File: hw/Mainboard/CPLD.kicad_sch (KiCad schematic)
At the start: 48 parts, among them J21 FPGA-P4, J22 Conn_02x15_Odd_Even, J23 FPGA_P2, J24 FPGA_P3, Q4 MMBT3904, SW5 CONFIG, U21 T8Q144C3, X1 50MHZ

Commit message: hw: wip
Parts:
- removed J22: Conn_02x15_Odd_Even, Connector_PinHeader_2.54mm:PinHeader_2x15_P2.54mm_Vertical, symbol Connector_Generic:Conn_02x15_Odd_Even
- added C82: 100n, Capacitor_SMD:C_0402_1005Metric, symbol Device:C_Small
- added J19: PROG, Connector_IDC:IDC-Header_2x08_P2.54mm_Vertical, symbol Connector_Generic:Conn_02x08_Odd_Even
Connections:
- net +3V3: now also C82.1, J19.1 (Pin_1)
- net CDONE: now also J19.10 (Pin_10)
- net GND: now also C82.2
- net NSTATUS: now also J19.5 (Pin_5)
- net SPI0_RX: now also J19.2 (Pin_2)
- net SPI0_SCK: now also J19.6 (Pin_6)
- net SPI0_TX: now also J19.4 (Pin_4)
- net SPI0_~{CS}: now also J19.8 (Pin_8)
- net TCK: now also RN14.3 (R3.1), J19.13 (Pin_13); no longer RN14.1 (R1.1)
- net TDI: now also RN14.4 (R4.1), J19.15 (Pin_15); no longer RN14.2 (R2.1)
- net TDO: now also RN14.1 (R1.1), J19.9 (Pin_9); no longer RN14.3 (R3.1)
- net TMS: now also RN14.2 (R2.1), J19.11 (Pin_11); no longer RN14.4 (R4.1)
- net ~{CRESET}: now also J19.12 (Pin_12)
- net ~{FPGA_PROG}: now also J19.16 (Pin_16)
- new net HOLD: J19.14 (Pin_14)
- new net PD_GND: J19.7 (Pin_7)
- no-connect marks 28 -> 29
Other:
- note added: "AD6"

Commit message: hw: larger schematic pages, routed w/netties
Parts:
- removed R48, R51, R63, R67: 10k, Resistor_SMD:R_0402_1005Metric, symbol Device:R_Small
- added RN15: 10k, Resistor_SMD:R_Array_Convex_4x0603, symbol Device:R_Pack04
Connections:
- net +3V3: now also J19.3 (Pin_3), RN15.5 (R4.2), RN15.6 (R3.2), RN15.7 (R2.2), RN15.8 (R1.2); no longer J19.1 (Pin_1)
- net CBUS0: now also RN15.1 (R1.1)
- net CBUS1: now also RN15.2 (R2.1)
- net CBUS2: now also RN15.3 (R3.1)
- net CSI: now also RN15.4 (R4.1)
- net SPI1_~{READY}: now also U21.18 (GPIOL_20_CTRL0_CDI4)
- no-connect marks 29 -> 30
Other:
- note added: "CDONE is open drain"
- note removed: "CDONE is an open drain"
- moved on the sheet: C59, C60, C61, C62, C63, C64, C65, C66, C67, C68, C69, C70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

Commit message: hw: wip
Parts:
- added NT39: +3V3, PET:NetTie-2_SMD_Pad_1.6_to_0.4mm, symbol PET:PowerTie_2
- added NT40, NT43, NT44: +3V3, PET:NetTie-2_SMD_Pad_0.4_to_0.28mm, symbol PET:PowerTie_2
- added PT3: PowerTie_2, PET:NetTie-2_SMD_Pad_1.6_to_0.4mm, symbol PET:PowerTie_2
- NT7, NT8: footprint PET:NetTie-2_SMD_Pad_0.4_to_0.2mm -> PET:NetTie-2_SMD_Pad_0.4_to_0.28mm; symbol Device:NetTie_2 -> PET:PowerTie_2
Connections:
- net +3V3: now also NT7.1, NT39.2, NT40.1, PT3.2; no longer NT7.2
- net FPGA_VCC: now also NT43.2, NT44.2
- net FPGA_VCCIO: now also NT7.2, NT40.2; no longer NT7.1
- net GRAPHICS: now also J23.14 (Pin_14), U21.45 (GPIOB_TXP06); no longer J23.13 (Pin_13), U21.43 (GPIOB_TXN04)
- net VIA_CB2: now also J23.13 (Pin_13), U21.43 (GPIOB_TXN04); no longer J23.14 (Pin_14), U21.45 (GPIOB_TXP06)
- net MCU_CEC: now reaches U21.33 (GPIOL_05_CSO)
- net ~{FPGA_PROG} renamed ~{SPI_ENA}
- new net +1V2: NT43.1, NT44.1
- new net PD_3V3: NT39.1, PT3.1
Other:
- note added: "Pull ~{CRESET} low to reset FPGA until MCU is ready Pull CSI high to enable FPGA configuration Pull TEST_N high to deactivate test mode Pull CBUS[2:0] high for 1x SPI width Leave CBSEL[1:0] floating (not using multi-image) MCU config: MCU drives SS_N low to select passive SPI MCU transitions CRESET_N low -> high to begin (320 ns) MCU sends bitsteam via CCK and CDI0 FPGA asserts CDONE on success, 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"
- note removed: "Pull CSI high to enable FPGA configuration Pull TEST_N high to deactivate test mode Pull CBUS[2:1] high as we don't support more than 2x Leave CBSEL[1:0] floating CRESET_N pulled low to reset FPGA until MCU is ready Config sequence: MCU drives CBUS[0] high for 1x or low for 2x MCU drives SS_N low to select passive SPI MCU transitions CRESET_N low -> high to begin (320 ns) MCU sends bitsteam via C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"
- note removed: "Pull ~{CRESET} low to suspend FPGA until MCU drives pin."
- note removed: "~{FPGA_PROG} transitions low during CRESET (before ~{SS}) and returns high after ~{SS} deasserts."
- moved on the sheet: C82, J19

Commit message: hw: wip
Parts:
- NT39, NT40, NT43, PT3: symbol PET:PowerTie_2 -> Device:NetTie_2
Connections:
- no-connect marks 30 -> 29
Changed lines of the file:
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@@
   (no_connect (at 246.38 109.22))
   (no_connect (at 311.15 132.08))
-  (no_connect (at 123.19 57.15))
   (no_connect (at 394.97 52.07))
   (no_connect (at 392.43 52.07))
@@
     (pin "1")
   )
-  (symbol (lib_id "PET:PowerTie_2") (at 100.33 147.32 0) (mirror y) (unit 1)
+  (symbol (lib_id "Device:NetTie_2") (at 100.33 147.32 0) (mirror y) (unit 1)
     (in_bom yes) (on_board yes)
     (property "Reference" "NT43" (id 0) (at 100.33 144.78 0)
@@
     (pin "2")
   )
-  (symbol (lib_id "PET:PowerTie_2") (at 33.02 162.56 0) (unit 1)
+  (symbol (lib_id "Device:NetTie_2") (at 33.02 162.56 0) (unit 1)
     (in_bom yes) (on_board yes) (fields_autoplaced)
     (property "Reference" "PT3" (id 0) (at 33.02 160.655 0)
@@
     (pin "1")
   )
-  (symbol (lib_id "PET:PowerTie_2") (at 33.02 160.02 0) (unit 1)
+  (symbol (lib_id "Device:NetTie_2") (at 33.02 160.02 0) (unit 1)
     (in_bom yes) (on_board yes)
     (property "Reference" "NT39" (id 0) (at 33.02 157.48 0)
@@
     (pin "1")
   )
-  (symbol (lib_id "PET:PowerTie_2") (at 44.45 162.56 0) (unit 1)
+  (symbol (lib_id "Device:NetTie_2") (at 44.45 162.56 0) (unit 1)
     (in_bom yes) (on_board yes)
     (property "Reference" "NT40" (id 0) (at 44.45 160.02 0)

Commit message: jlcpcb - 1/19
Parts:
- removed JP10: TRI, Jumper:SolderJumper-2_P1.3mm_Open_RoundedPad1.0x1.5mm, symbol Jumper:SolderJumper_2_Open
- removed NT40, NT43: +3V3, PET:NetTie-2_SMD_Pad_0.4_to_0.28mm, symbol Device:NetTie_2
- removed NT7: +3V3, PET:NetTie-2_SMD_Pad_0.4_to_0.28mm, symbol PET:PowerTie_2
- C59, C65, C66, C67, C68, C77, C78, C79, C80: value 10n -> 10n 50V
- C60, C69, C70: value 1u -> 1u 25V
- D8: value GRN_DONE -> LED_GRN
- D9: value RED_STATUS -> LED_RED
- J21, J23, J24: MOUSER 517-929975-01-14 -> (none)
- R27, R32, R33: LCSC C25077 -> C25744
- U21: DIGI-KEY (none) -> 2134-T8Q144C3-ND; MANUFACTURER Efinix -> (none); MAXIMUM_PACKAGE_HEIGHT 1.6mm -> (none); MPN (none) -> T8Q144C3; PARTREV V3.6 -> (none); STANDARD IPC-7351B -> (none)
- X1: value 50MHZ -> 50 MHz
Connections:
- net FPGA_VCCIO is gone; now on net +3V3: C69.1, C70.1, C71.1, C72.1, C73.1, C74.1, C75.1, C76.1, C77.1, C78.1, C79.1, C80.1, U21.12 (VCCIO1C_1D), U21.122 (VCCIO3A), U21.143 (VCCIO1E), U21.21 (VCCIO1B), U21.23 (VCCIO1A), U21.51 (VCCIO4B), U21.52 (VCCIO4B), U21.62 (VCCIO4A), U21.63 (VCCIO4A), U21.88 (VCCIO3E), U21.91 (VCCIO3D), U21.95 (VCCIO3B_3C)
- net GND: now also J21.13 (Pin_13), J21.14 (Pin_14), J23.3 (Pin_3)
- net S3: now also U21.137 (GPIOL_70_CBSEL0); no longer U21.139 (GPIOL_68)
- net S4: now also U21.138 (GPIOL_69_CBSEL1); no longer U21.140 (GPIOL_67_CDI13)
- net R76: now reaches J21.11 (Pin_11)
- net R76: now also U21.124 (GPIOR_76_PLLIN0)
- net 50M_ENA: now reaches J21.12 (Pin_12)
- net 50M_ENA: now also X1.1 (Tri-State)
- net L65: now reaches J21.23 (Pin_23)
- net L65: now also U21.141 (GPIOL_65)
- net L64: now reaches J21.25 (Pin_25)
- net L64: now also U21.144 (GPIOL_64)
- net L66: now reaches J21.26 (Pin_26)
- net L66: now also U21.142 (GPIOL_66_CDI12)
- net S5 renamed L68
- net L68: now also U21.139 (GPIOL_68); no longer U21.141 (GPIOL_65)
- net S6 renamed L67
- net L67: now also U21.140 (GPIOL_67_CDI13); no longer U21.142 (GPIOL_66_CDI12)
- net X1 renamed N02
- net X2 renamed P02
- net X3 renamed N00
- no-connect marks 29 -> 17

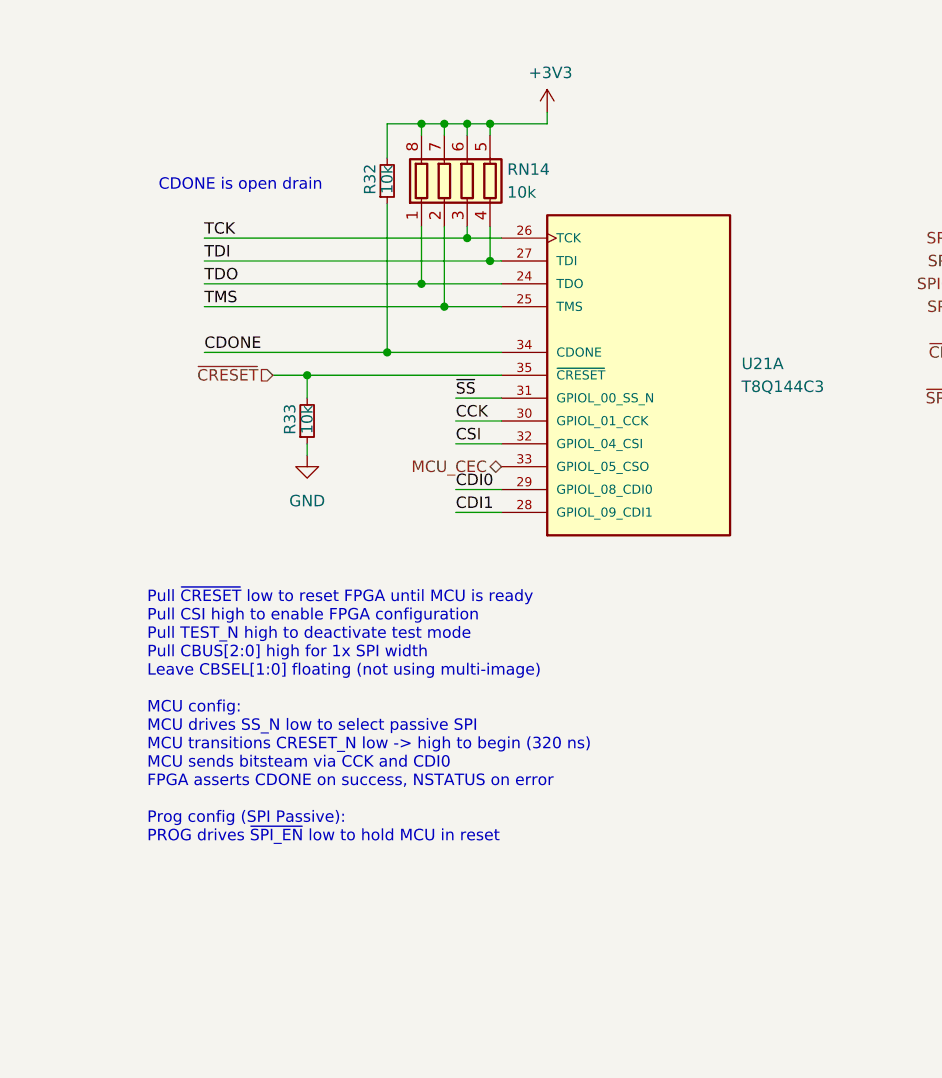
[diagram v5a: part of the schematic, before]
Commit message: hw: drive CRESET through 10k, remove TDO pullup
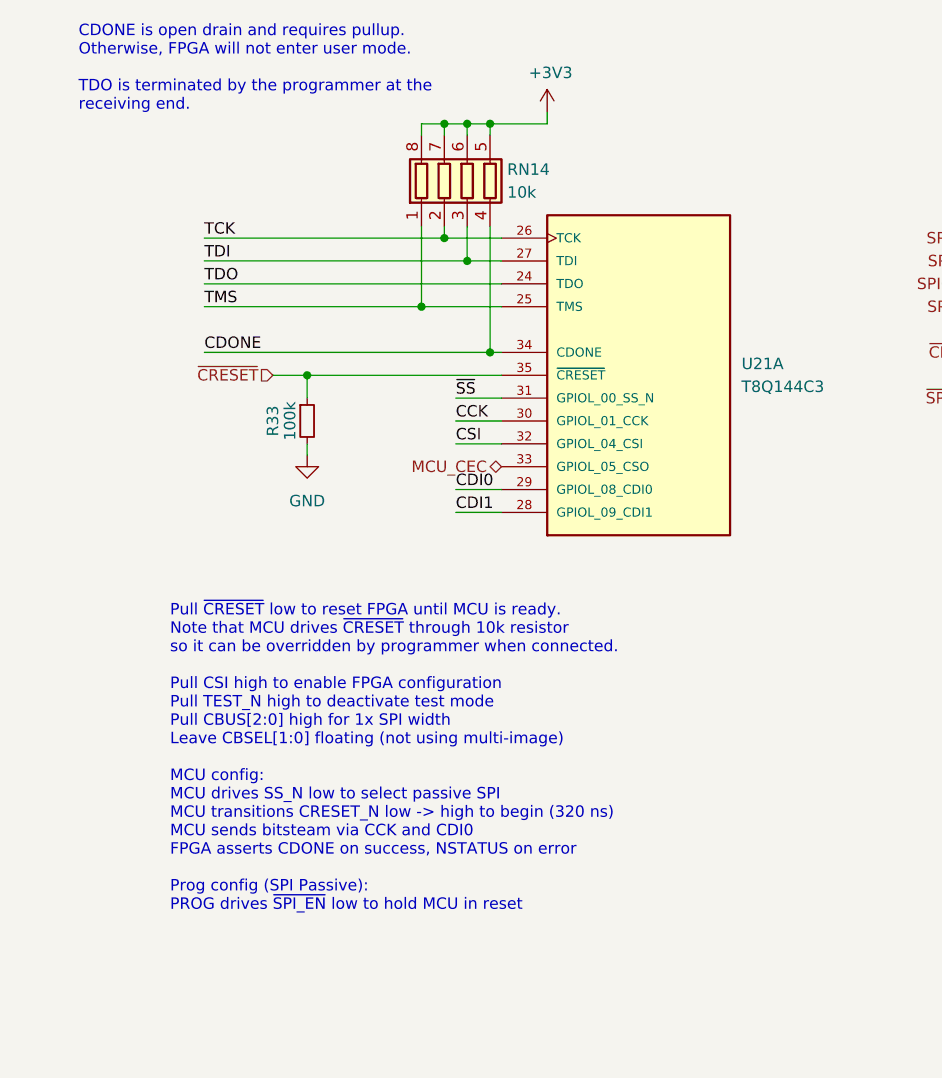
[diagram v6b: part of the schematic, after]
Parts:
- removed R32: 10k, Resistor_SMD:R_0402_1005Metric, symbol Device:R_Small
- R33: value 10k -> 100k; LCSC C25744 -> C25741
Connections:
- net CDONE: now also RN14.4 (R4.1)
- net GND: now also R33.2; no longer R33.1
- net TCK: now also RN14.2 (R2.1); no longer RN14.3 (R3.1)
- net TDI: now also RN14.3 (R3.1); no longer RN14.4 (R4.1)
- net TDO: no longer RN14.1 (R1.1)
- net TMS: now also RN14.1 (R1.1); no longer RN14.2 (R2.1)
- net ~{CRESET}: now also R33.1; no longer R33.2
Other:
- note added: "CDONE is open drain and requires pullup. Otherwise, FPGA will not enter user mode. TDO is terminated by the programmer at the receiving end."
- note added: "Pull ~{CRESET} low to reset FPGA until MCU is ready. Note that MCU drives ~{CRESET} through 10k resistor so it can be overridden by programmer when connected. Pull CSI high to enable FPGA configuration Pull TEST_N high to deactivate test mode Pull CBUS[2:0] high for 1x SPI width Leave CBSEL[1:0] floating (not using multi-image) MCU config: MCU drives SS_N low to select passive SPI MCU transitions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"
- note removed: "CDONE is open drain"
- note removed: "Pull ~{CRESET} low to reset FPGA until MCU is ready Pull CSI high to enable FPGA configuration Pull TEST_N high to deactivate test mode Pull CBUS[2:0] high for 1x SPI width Leave CBSEL[1:0] floating (not using multi-image) MCU config: MCU drives SS_N low to select passive SPI MCU transitions CRESET_N low -> high to begin (320 ns) MCU sends bitsteam via CCK and CDI0 FPGA asserts CDONE on success, 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"

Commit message: hw: pin 1 of 50 MHz oscillator can float
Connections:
- net GND: now also J21.12 (Pin_12)
- net 50M_ENA: no longer names the net of X1.1 (Tri-State)
- net 50M_ENA: no longer J21.12 (Pin_12)
- no-connect marks 17 -> 18
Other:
- note added: "Floating pin 1 enables CLK_50 Grounding pin 1 suspends CLK_50"
